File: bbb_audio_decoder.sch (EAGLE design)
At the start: 180 parts, among them IC1 OPA2134, IC2 LM317, IC3 LM337, IC4 OPA2134, IC5 OPA2134, IC6 OPA2134, P1 PLR135/T9, Q2 BS170, U1 PCM1690, U2 DIR9001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

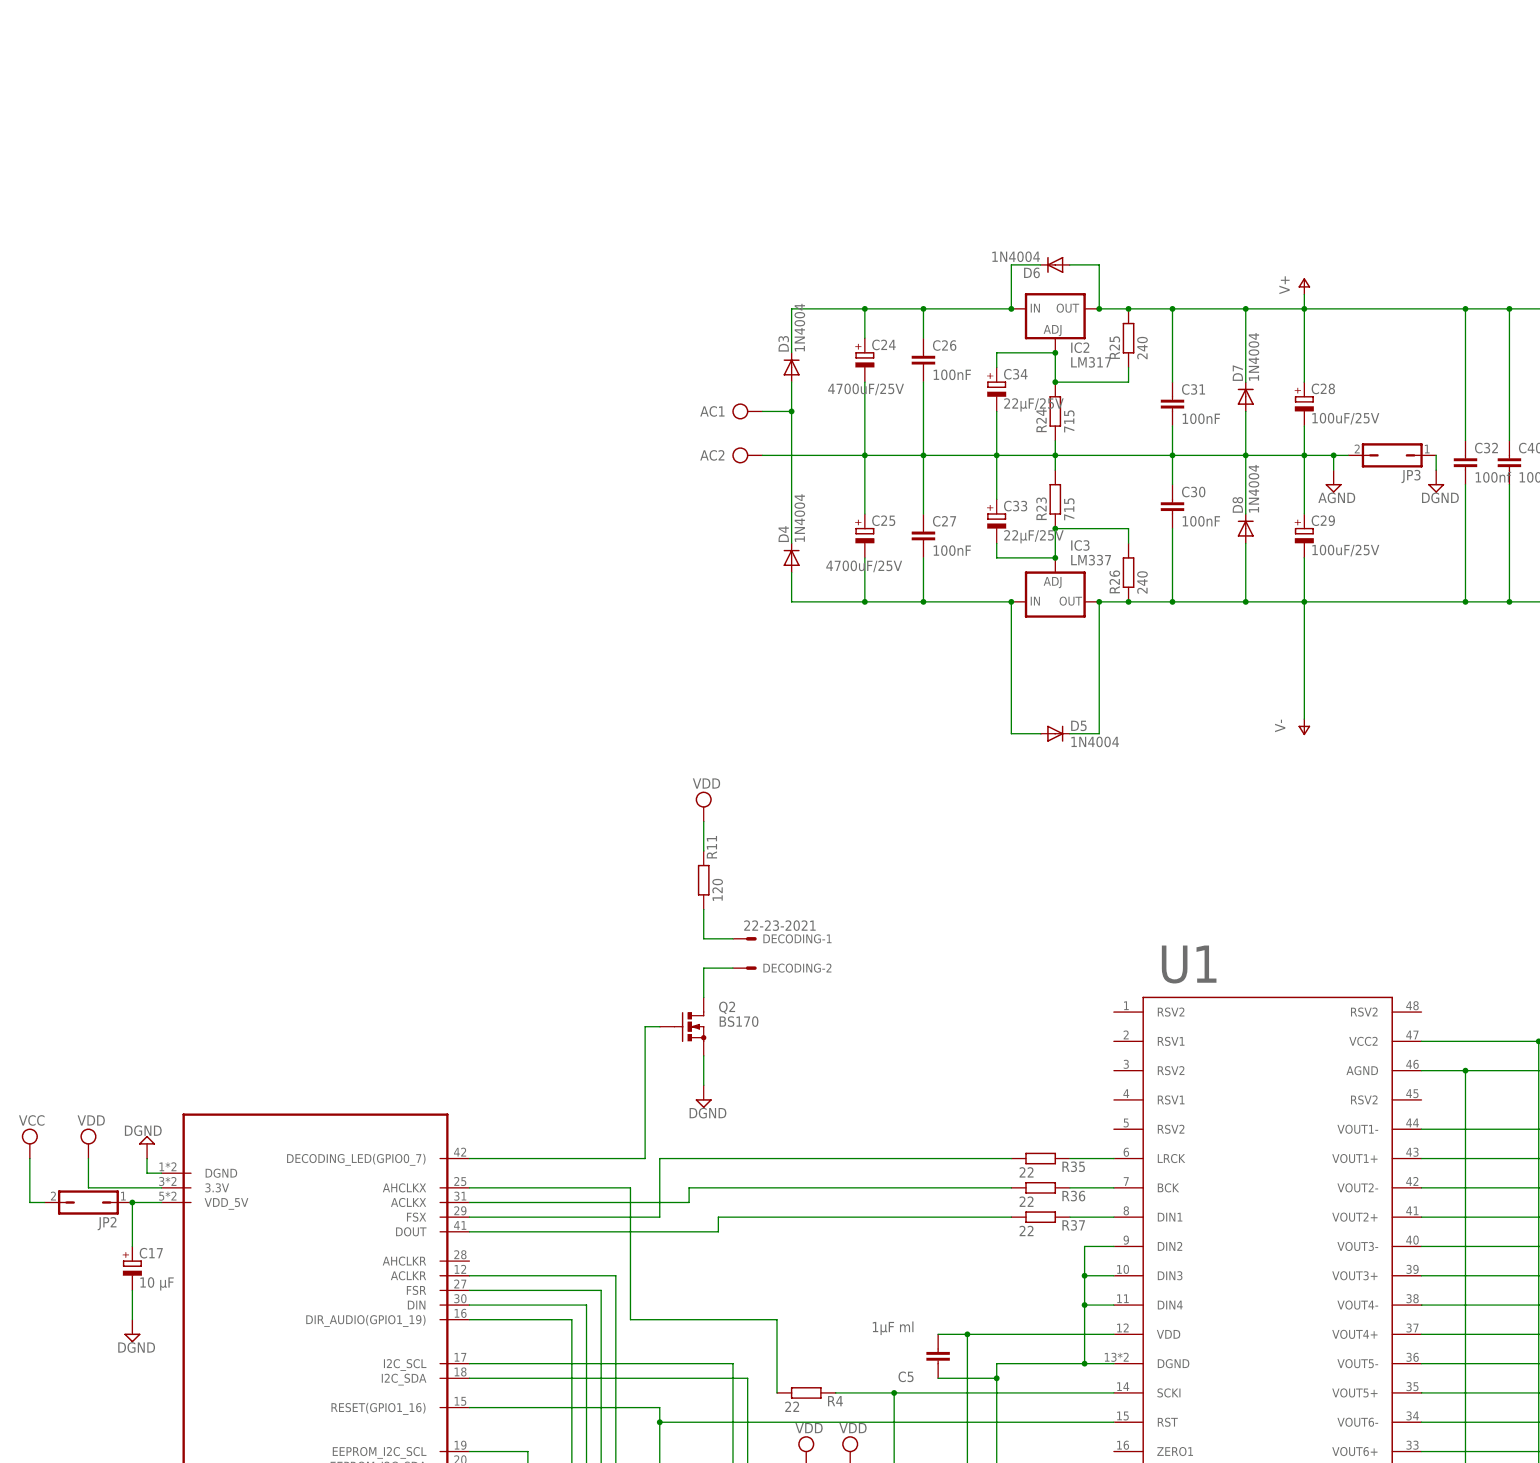
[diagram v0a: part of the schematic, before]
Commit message: Included LM317 voltage regulator for Beagle Bone
This is the power supply for it, removing the need for a power adapter
for it.

This also changes the AC input to needing a dual winding transformer. My
idea of univeral adapters was nice, until AC "wall warts" became illegal
because of energy laws... Plus, I reduced the supply caps, so I need the
full-wave rectifier now.

I also removed the jumpers to choose to feed the Beagle Bone from the
analog power supply. This was an idea that was never going to work, it
was clear early on. Current demand of one LM317 was too high, and it
would make the analog supply noisy.
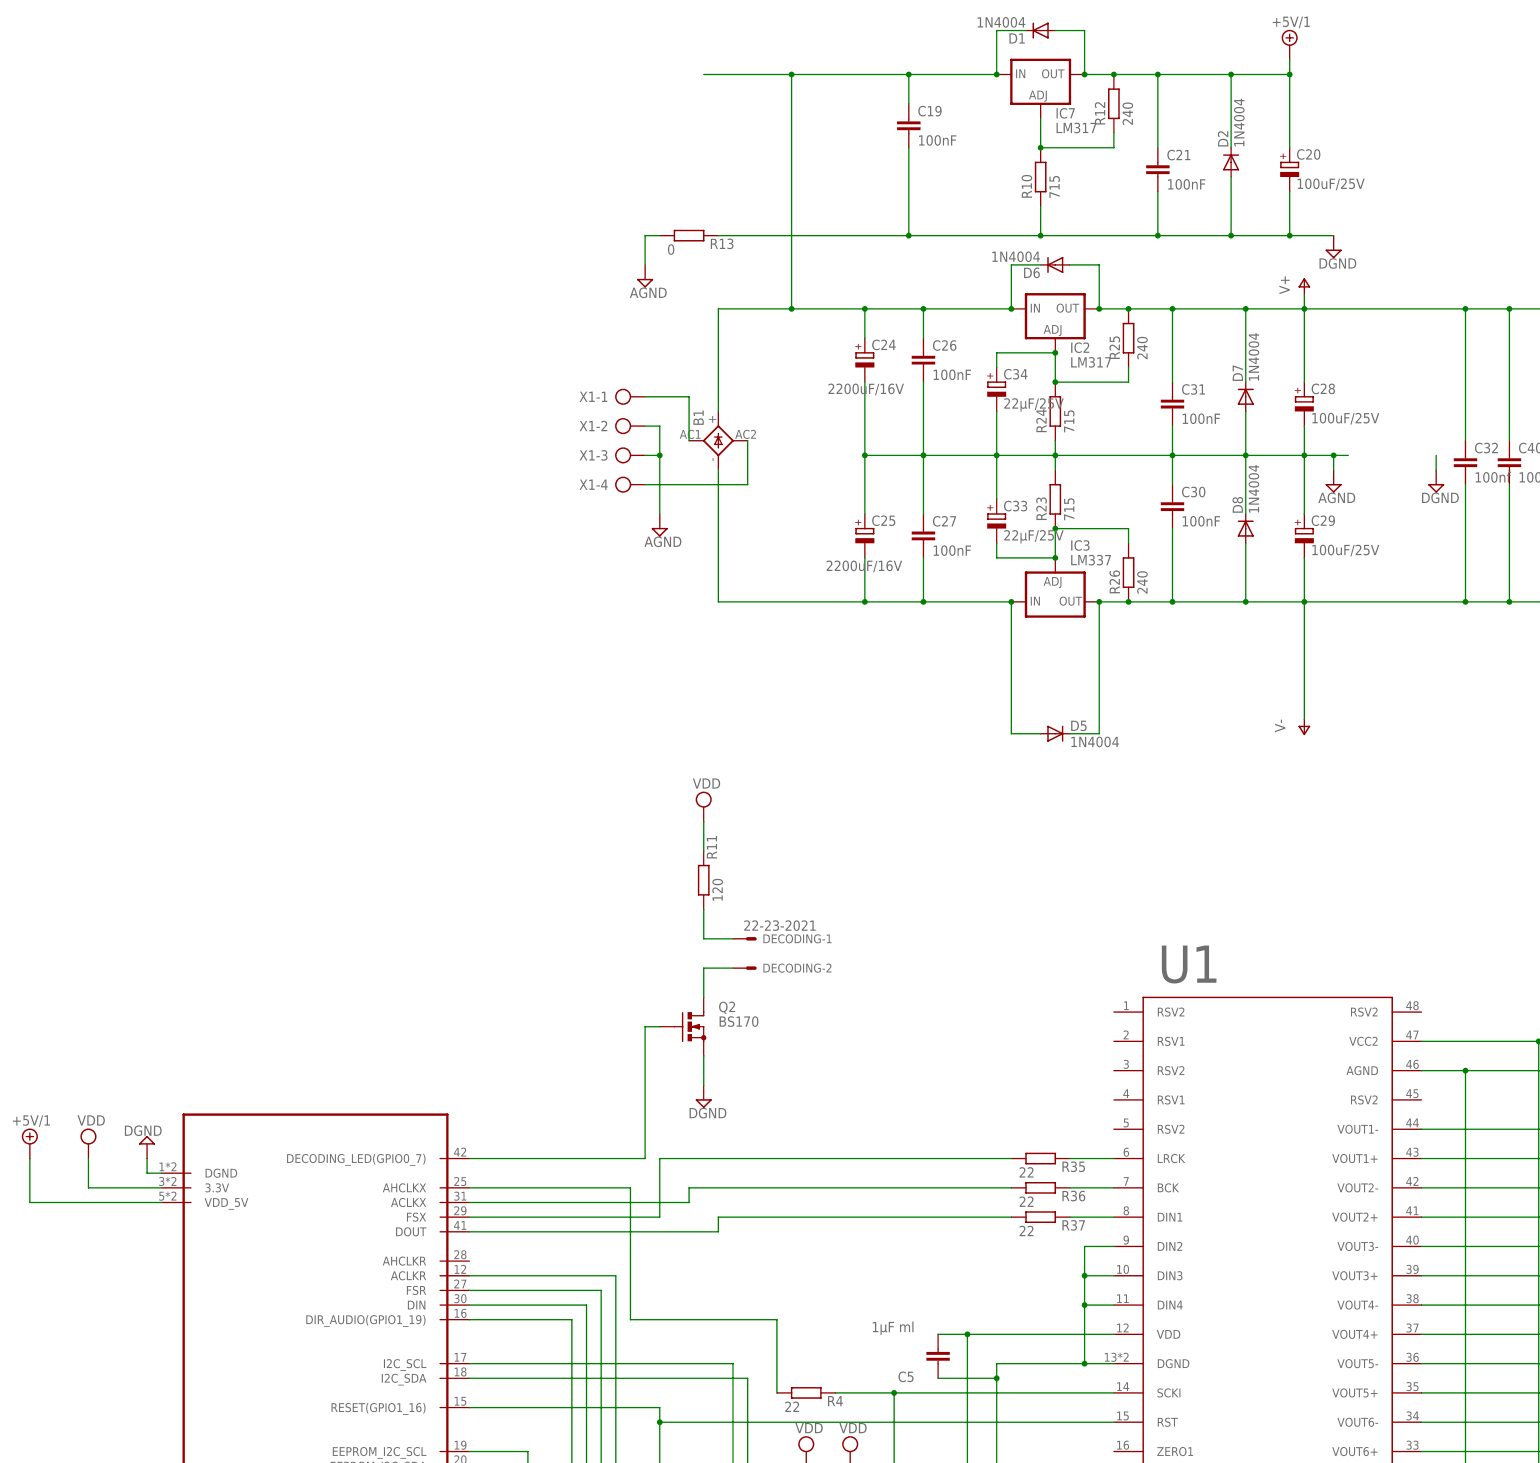
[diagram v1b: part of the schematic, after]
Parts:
- removed AC: ADAPTER-PLUG-5.5/2.1MM, 0000halfgaar:ADAPTER-PLUG-5.5/2.1MM
- removed C17: 10 µF, rcl:CPOL-EUE2-5
- removed D3, D4: 1N4004, diode:DIODE-DO41-7.6
- removed JP2, JP3: (no value), jumper:JP1Q
- added B1: (no value), rectifier:FB15
- added C19, C21: 100nF, rcl:C-EU050-024X044
- added C20: 100uF/25V, rcl:CPOL-EUE2.5-6
- added D1, D2: 1N4004, diode:DIODE-DO41-7.6
- added IC7: LM317, v-reg:LM317TS
- added R10: 715, rcl:R-EU_0204/2V
- added R12: 240, rcl:R-EU_0204/2V
- added R13: 0, rcl:R-EU_0204/2V
- added X1: (no value), con-ptr500:AK500/4
- C24, C25: value 4700uF/25V -> 2200uF/16V; device rcl:CPOL-EUE7.5-16 -> rcl:CPOL-EUE5-13
- R23, R25, R26: device rcl:R-EU_0207/10 -> rcl:R-EU_0204/2V
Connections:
- new net N$1: B1.AC2, X1-4.KL
- new net N$3: B1.AC1, X1-1.KL
- net AGND: now also R13.1, X1-2.KL, X1-3.KL; no longer AC2.KL, JP3.2
- net DGND: now also C19.2, C20.-, C21.2, D2.A, R10.1, R13.2; no longer C17.-, JP3.1
- net N$39: now also B1.+, C19.1, D1.C, IC7.IN; no longer D3.C
- net N$40: now also IC7.ADJ, R10.2, R12.1; no longer AC1.KL, D3.A, D4.C
- net N$41: now also B1.-; no longer D4.A
- net VCC: no longer JP2.2
- net VDD_5V: now also C20.+, C21.1, D1.A, D2.C, IC7.OUT, R12.2; no longer C17.+, JP2.1
